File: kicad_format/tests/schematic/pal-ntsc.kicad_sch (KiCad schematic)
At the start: 36 parts, among them U10 BT812, X2 30MHz

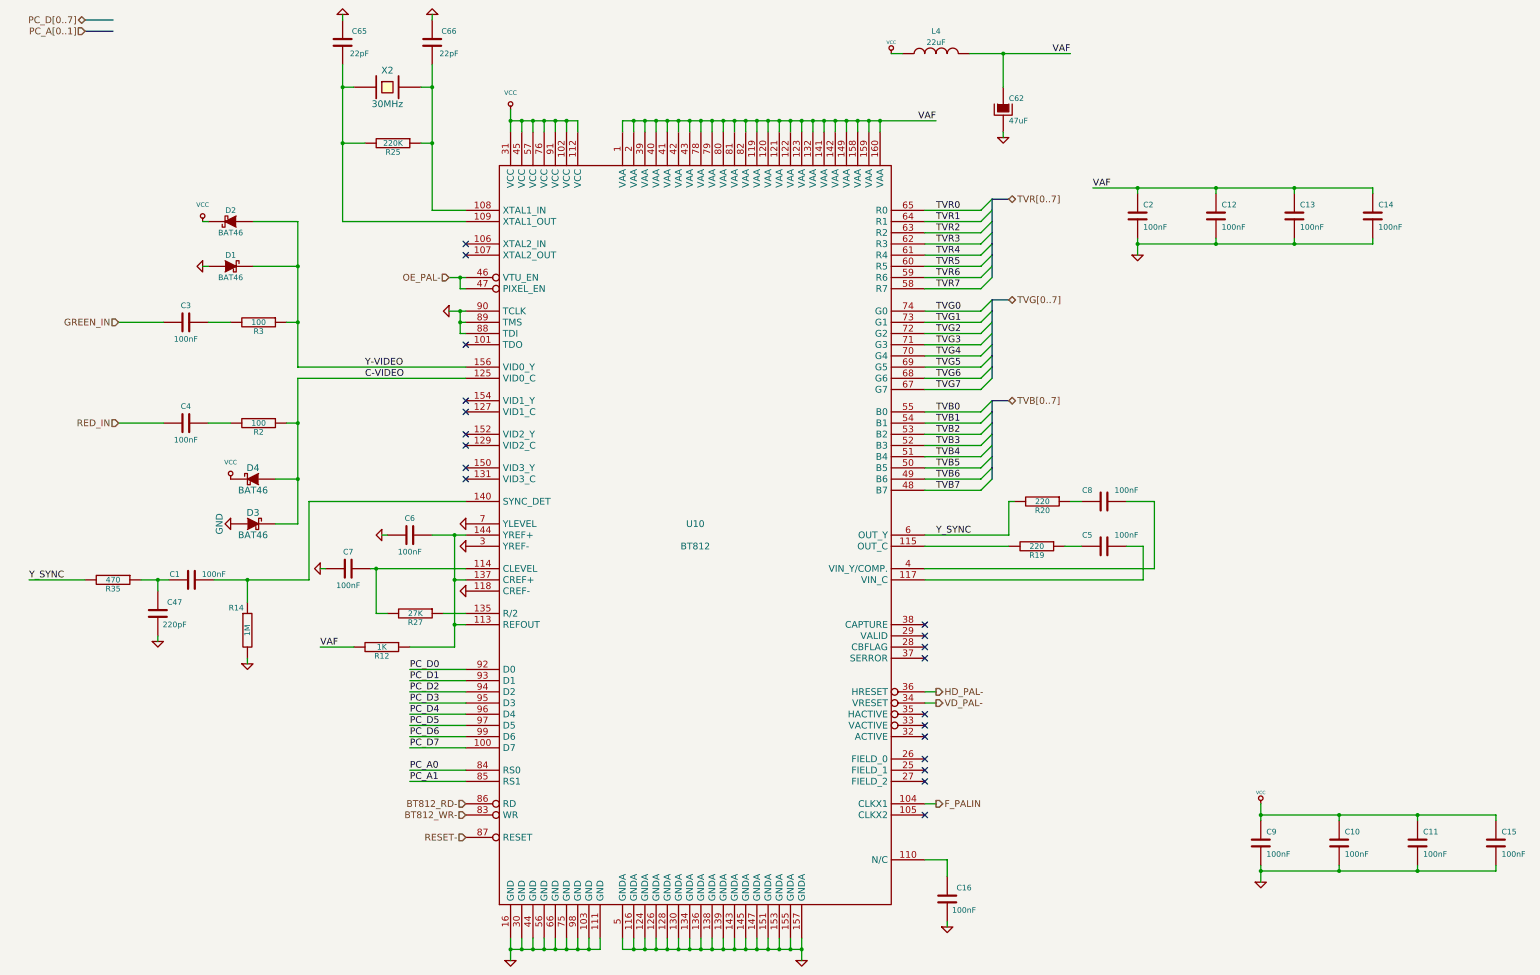
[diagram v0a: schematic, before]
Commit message: Add serialization context and support most modern kicad file idiosyncrasies
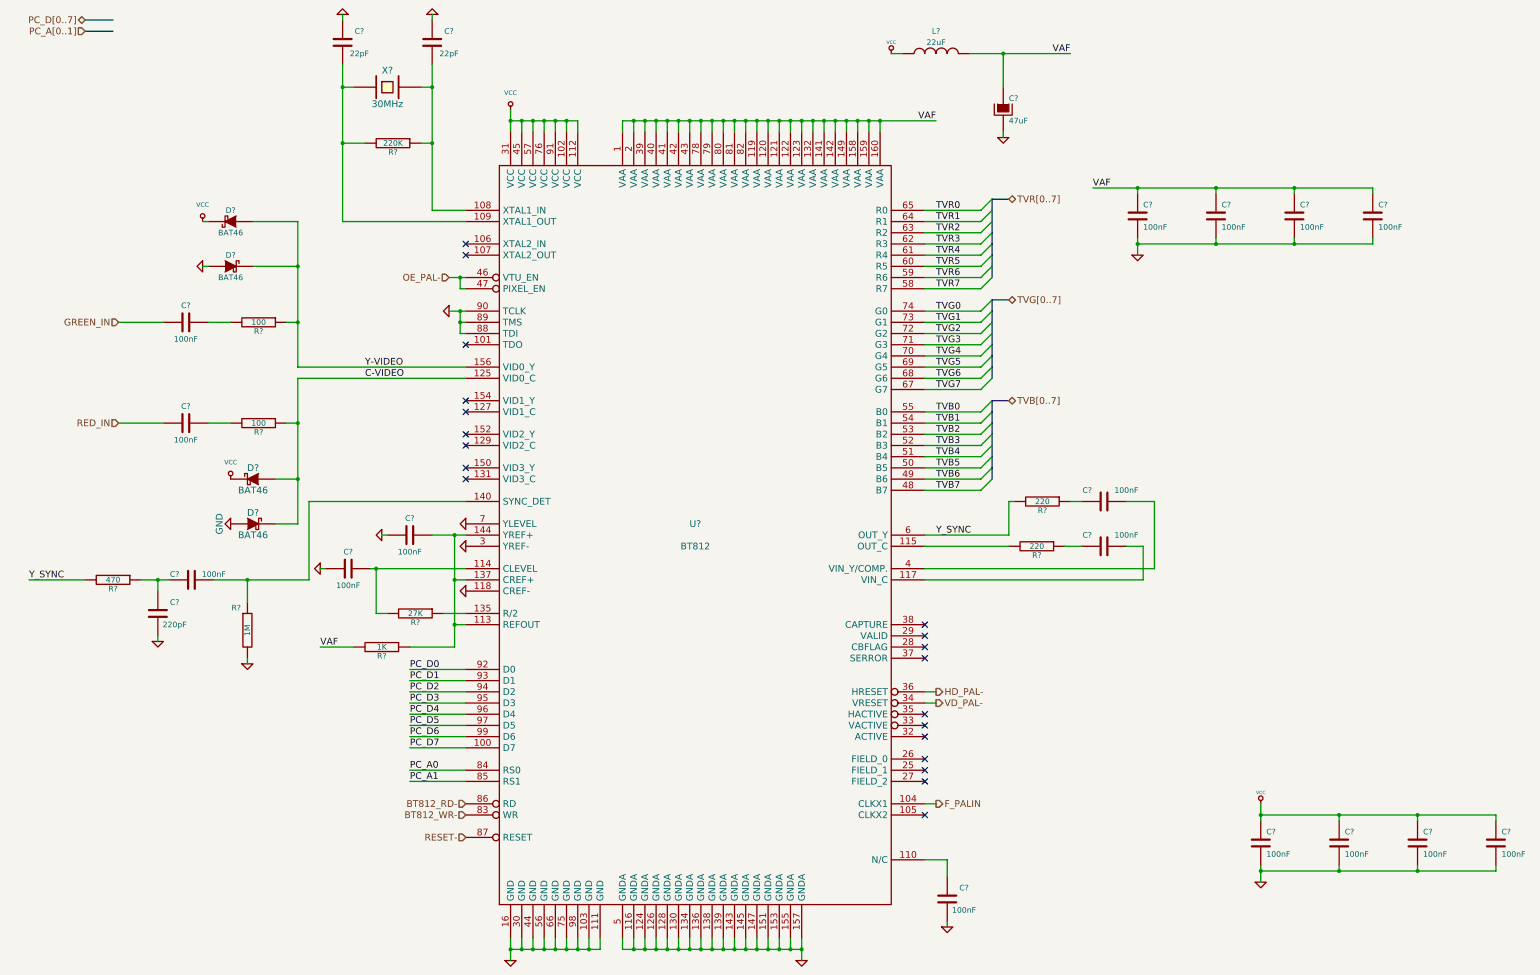
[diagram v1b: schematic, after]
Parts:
- renumbered C15 to C?, C16 to C?, C66 to C?, C11 to C?, C14 to C?, C47 to C?, C4 to C?, C6 to C?, C3 to C?, C5 to C?, C62 to C?, C2 to C?, C10 to C?, C13 to C?, C12 to C?, C1 to C?, C7 to C?, C9 to C?, C8 to C?, C65 to C?, D2 to D?, D1 to D?, D3 to D?, D4 to D?, L4 to L?, R25 to R?, R2 to R?, R35 to R?, R19 to R?, R12 to R?, R20 to R?, R27 to R?, R14 to R?, R3 to R?, U10 to U?, X2 to X?
